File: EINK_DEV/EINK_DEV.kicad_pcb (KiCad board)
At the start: 2 copper layers, 50.5 x 46.5 mm, 76 parts, among them J1 FPC, J2 Conn_01x06, J3 Conn_01x02, J4 Conn_01x03, J5 Conn_ARM_SWD_TagConnect_TC2030, J6 UART, J7 Conn_Coaxial, J8 GPIO_Header_Dev, P1 USB_C_Plug_USB2.0, Q1 Si1304BDL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

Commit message: PCB gotowa
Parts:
- added J9: USER2, Connector_PinHeader_2.54mm:PinHeader_1x04_P2.54mm_Vertical, F.Cu at (127.5, 72.0)
- C1, C2, D2, L1: moved to B.Cu
- C10, C12, C31, C32, C5, C6, C7, C8, C9, R1, R2: moved to F.Cu
- FL1: value 2,4Ghz LP 50Ohm -> LP
- J2: value Conn_01x06 -> UART1; footprint Connector_PinHeader_2.54mm:PinHeader_1x06_P2.54mm_Vertical -> Connector_PinHeader_2.54mm:PinHeader_1x04_P2.54mm_Vertical
- J6: value UART -> LPUART
- J7: value Conn_Coaxial -> SMD
- J8: value GPIO_Header_Dev -> USER1
- JP1: footprint Connector_PinHeader_2.54mm:PinHeader_1x03_P2.54mm_Vertical -> Connector_PinHeader_2.54mm:PinHeader_1x03_P2.54mm_Horizontal
- Q1: value Si1304BDL -> NMOS
- TH1: value Thermistor_NTC -> THRMST
- moved C3 38.5 mm to (158.2, 114.5)
- moved D1 36.5 mm to (155.0, 110.8), turned to 90 degrees
- moved SW1 32.9 mm to (136.0, 104.0), turned to 180 degrees
- moved D3 31.6 mm to (162.6, 104.7)
- moved R13 29.9 mm to (123.7, 104.5), turned to 0 degrees
- moved C30 28.4 mm to (123.7, 107.0), turned to 180 degrees
- moved J6 28.2 mm to (119.5, 99.5), turned to 0 degrees
- moved R12 26.4 mm to (123.7, 102.0), turned to 0 degrees
- moved C4 26.0 mm to (162.5, 100.8), turned to -90 degrees
- moved J2 25.3 mm to (127.5, 87.0), turned to 0 degrees
- moved R15 25.1 mm to (128.7, 107.0), turned to 0 degrees
- moved R10 23.3 mm to (176.5, 75.7), turned to 90 degrees
- moved TH1 18.7 mm to (178.0, 103.2), turned to 90 degrees
- moved J8 13.5 mm to (119.5, 72.0)
- moved R1 12.1 mm to (175.5, 104.7), turned to 90 degrees
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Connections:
- J2 pad 1: Net-(J2-Pin_1) -> +3.3V
- J2 pad 4: Net-(J2-Pin_4) -> GND
- U1 pad 13: Net-(J2-Pin_2) -> Net-(J9-Pin_2)
- U1 pad 14: Net-(J2-Pin_3) -> Net-(J9-Pin_3)
- U1 pad 18: Net-(J2-Pin_4) -> Net-(J2-Pin_2)
- U1 pad 36: Net-(J2-Pin_5) -> Net-(J2-Pin_3)
- U1 pad 42: Net-(J2-Pin_6) -> Net-(J9-Pin_4)
- U1 pad 9: Net-(J2-Pin_1) -> Net-(J9-Pin_1)
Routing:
- net GND: track 274.2 -> 371.3 mm, vias 4 -> 9
- net Net-(J8-Pin_2): track 0.00 -> 73.5 mm, vias 0 -> 1
- net Net-(U1-PA3): track 0.00 -> 69.4 mm, vias 0 -> 1
- net Net-(J9-Pin_3): track 0.00 -> 60.7 mm, vias 0 -> 3
- net +3V3: track 115.2 -> 172.1 mm, vias 5 -> 12
- net Net-(J8-Pin_9): track 0.00 -> 51.3 mm, vias 0 -> 2
- net Net-(J5-SWO): track 0.00 -> 49.4 mm, vias 0 -> 1
- net Net-(J8-Pin_3): track 2.08 -> 51.0 mm, vias 0 -> 1
- net D+: track 0.00 -> 48.0 mm, vias 0 -> 2
- net Net-(D1-A): track 9.30 -> 56.9 mm, vias 0 -> 4
- net Net-(U1-PA2): track 0.00 -> 47.4 mm, vias 0 -> 1
- net Net-(J9-Pin_2): track 0.00 -> 47.1 mm, vias 0 -> 2
- net RESE: track 59.9 -> 12.8 mm, vias 2 -> 0
- net Net-(J9-Pin_1): track 0.00 -> 46.7 mm, vias 0 -> 2
- net D-: track 0.00 -> 46.5 mm, vias 0 -> 2
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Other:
- board size 50.5 x 46.5 mm -> 66.5 x 48.5 mm

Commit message: update
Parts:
- J3: footprint Connector_Molex:Molex_KK-254_AE-6410-02A_1x02_P2.54mm_Vertical -> Connector_PinHeader_2.54mm:PinHeader_1x02_P2.54mm_Vertical
- J4: footprint Connector:FanPinHeader_1x03_P2.54mm_Vertical -> Connector_PinHeader_2.54mm:PinHeader_1x03_P2.54mm_Horizontal
- U2 >: renamed from U2
- moved J4 0.23 mm to (178.5, 91.9), turned to 0 degrees
- turned J3 to -90 degrees
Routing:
- net Net-(J8-Pin_2): track 73.5 -> 56.4 mm
- net GND: track 371.3 -> 368.6 mm

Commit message: Uporzadkowanie komponentów HF
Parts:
- C1, C17, C18, C2, C26, C27, C30, C33, D2, L1, R12, R13, R15, Y1: moved to F.Cu
- FL1: value LP -> 2,4Ghz LP 50Ohm
- J3: footprint Connector_PinHeader_2.54mm:PinHeader_1x02_P2.54mm_Vertical -> Connector_Molex:Molex_KK-254_AE-6410-02A_1x02_P2.54mm_Vertical
- J4: footprint Connector_PinHeader_2.54mm:PinHeader_1x03_P2.54mm_Horizontal -> Connector:FanPinHeader_1x03_P2.54mm_Vertical
- J5: footprint Connector:Tag-Connect_TC2030-IDC-FP_2x03_P1.27mm_Vertical -> Connector_PinHeader_2.54mm:PinHeader_1x06_P2.54mm_Vertical
- J6: value LPUART -> LOW POWER UART
- J7: value SMD -> Conn_Coaxial
- Q1: value NMOS -> Si1304BDL
- TH1: value THRMST -> Thermistor_NTC
- U2: renamed from U2 >
- moved JP1 109.3 mm to (70.5, 99.8), turned to 180 degrees
- moved P1 106.5 mm to (73.4, 72.9), turned to 90 degrees
- moved R4 101.9 mm to (71.9, 87.2), turned to 180 degrees
- moved R10 99.9 mm to (76.8, 70.3), turned to -90 degrees
- moved D4 99.8 mm to (72.0, 91.0), turned to 0 degrees
- moved C12 99.5 mm to (74.8, 83.7), turned to -90 degrees
- moved C31 99.2 mm to (81.8, 68.8), turned to 90 degrees
- moved R9 98.1 mm to (77.0, 74.6), turned to 90 degrees
- moved R5 97.0 mm to (76.8, 83.8)
- moved C32 96.4 mm to (80.2, 68.8)
- moved J4 96.3 mm to (82.4, 98.5)
- moved J3 95.3 mm to (74.5, 99.0), turned to 0 degrees
- moved U2 94.1 mm to (79.2, 88.2), turned to 180 degrees
- moved TH1 93.8 mm to (84.8, 93.5), turned to 180 degrees
- moved U3 93.5 mm to (80.7, 73.6)
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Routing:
- net GND: track 368.6 -> 0.00 mm, vias 9 -> 0
- net +3V3: track 172.1 -> 0.00 mm, vias 12 -> 0
- net Net-(J2-Pin_2): track 75.6 -> 0.00 mm, vias 7 -> 0
- net Net-(D4-A): track 75.0 -> 0.00 mm, vias 7 -> 0
- net Net-(U1-PA3): track 69.4 -> 0.00 mm, vias 1 -> 0
- net Net-(D3-A): track 63.5 -> 0.00 mm, vias 1 -> 0
- net VBUS: track 61.0 -> 0.00 mm, vias 4 -> 0
- net Net-(J9-Pin_3): track 60.7 -> 0.00 mm, vias 3 -> 0
- net Net-(D1-A): track 56.9 -> 0.00 mm, vias 4 -> 0
- net Net-(J8-Pin_2): track 56.4 -> 0.00 mm, vias 1 -> 0
- net Net-(J8-Pin_7): track 53.6 -> 0.00 mm, vias 3 -> 0
- net Net-(J8-Pin_9): track 51.3 -> 0.00 mm, vias 2 -> 0
- net Net-(J8-Pin_3): track 51.0 -> 0.00 mm, vias 1 -> 0
- net Net-(J5-SWO): track 49.4 -> 0.00 mm, vias 1 -> 0
- net Net-(J8-Pin_1): track 49.3 -> 0.00 mm, vias 1 -> 0
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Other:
- board outline removed
- copper layers 2 -> 4

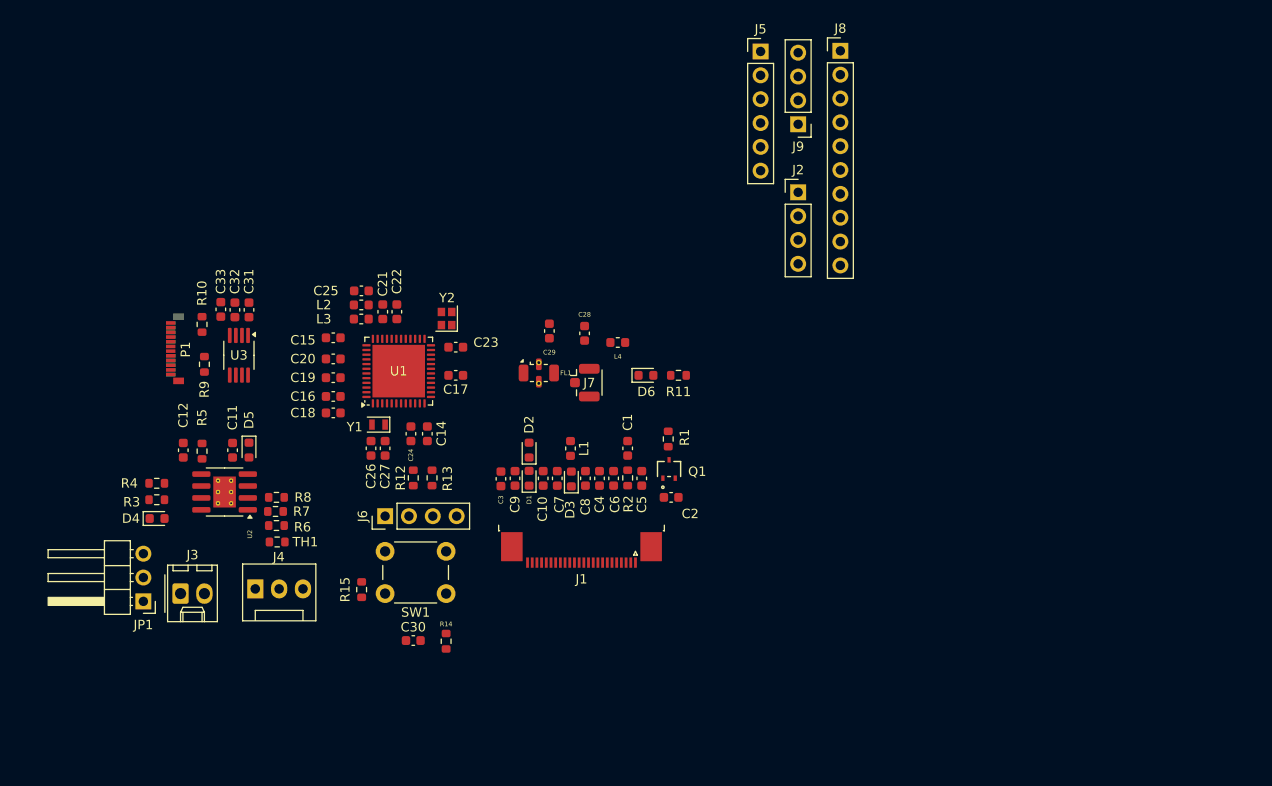
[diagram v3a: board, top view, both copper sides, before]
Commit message: Płytka prawie końcowa
 - prawidłowa impredancja
- prawidłowe warstwy GND i 3v3
- rozłożenie prawidłowe C 
- do poprawienia napisy
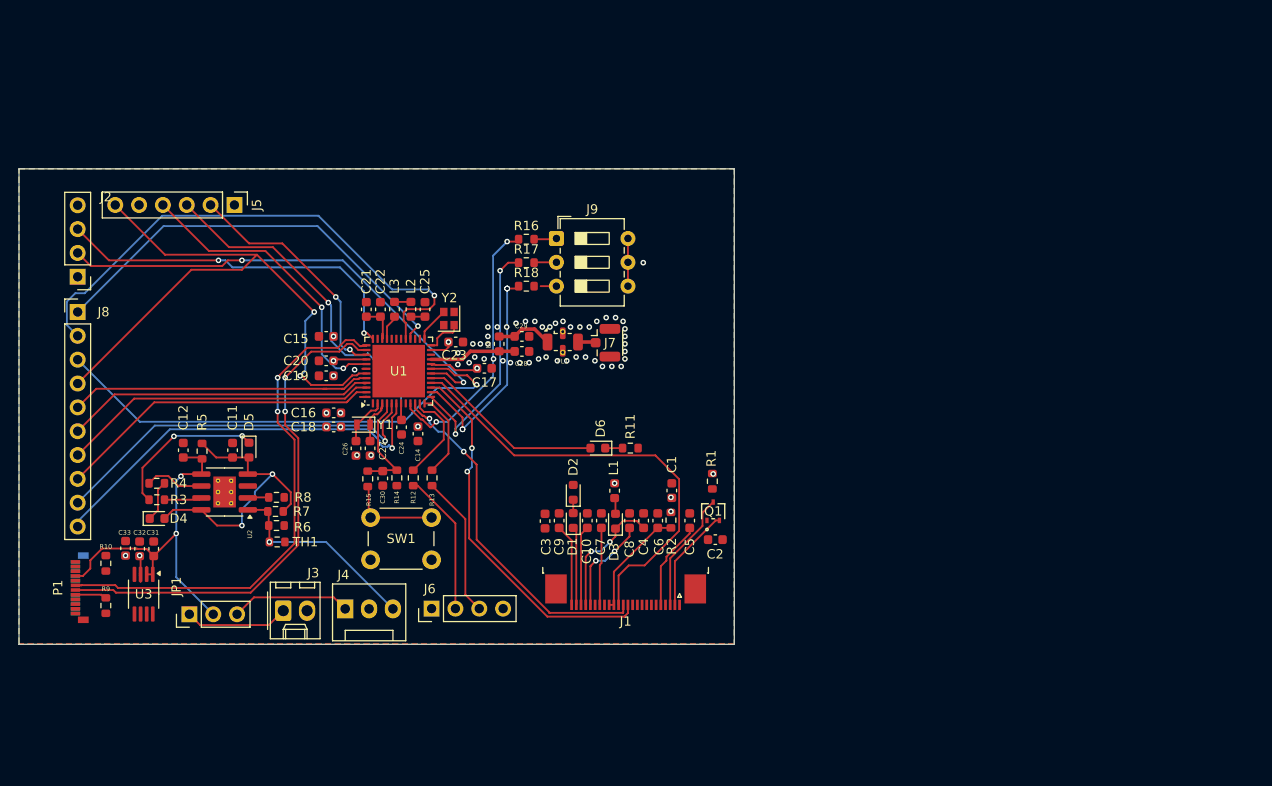
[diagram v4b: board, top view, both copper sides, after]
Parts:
- added R16: 220R, Resistor_SMD:R_0603_1608Metric, F.Cu at (111.3, 61.2)
- added R17: 220R, Resistor_SMD:R_0603_1608Metric, F.Cu at (111.3, 63.8)
- added R18: 220R, Resistor_SMD:R_0603_1608Metric, F.Cu at (111.3, 66.2)
- J9: footprint Connector_PinHeader_2.54mm:PinHeader_1x04_P2.54mm_Vertical -> Button_Switch_THT:SW_DIP_SPSTx03_Slide_6.7x9.18mm_W7.62mm_P2.54mm_LowProfile
- JP1: footprint Connector_PinHeader_2.54mm:PinHeader_1x03_P2.54mm_Horizontal -> Connector_PinHeader_2.54mm:PinHeader_1x03_P2.54mm_Vertical
- moved J8 85.9 mm to (63.5, 69.0)
- moved J2 77.3 mm to (63.5, 65.2), turned to 180 degrees
- moved J5 58.4 mm to (80.2, 57.6), turned to -90 degrees
- moved J9 28.5 mm to (114.5, 61.2), turned to 0 degrees
- moved R9 27.8 mm to (66.5, 100.3)
- moved R10 27.4 mm to (66.5, 95.8)
- moved C33 27.4 mm to (68.6, 94.2)
- moved P1 27.4 mm to (63.2, 98.4)
- moved U3 27.4 mm to (70.5, 99.1)
- moved C31 27.4 mm to (71.6, 94.2)
- moved C32 27.4 mm to (70.1, 94.2)
- moved R14 18.2 mm to (97.5, 86.7)
- moved C30 17.6 mm to (96.0, 86.7), turned to -90 degrees
- moved L4 12.6 mm to (108.4, 72.4), turned to 90 degrees
- moved R15 11.8 mm to (94.4, 86.8)
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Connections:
- J2 pad 1: +3.3V -> +3V3
- J6 pad 1: +3.3V -> +3V3
- J9 pad 1: Net-(J9-Pin_1) -> Net-(J9-Pad1)
- J9 pad 2: Net-(J9-Pin_2) -> Net-(J9-Pad2)
- J9 pad 3: Net-(J9-Pin_3) -> Net-(J9-Pad3)
- J9 pad 4: Net-(J9-Pin_4) -> +3V3
- SW1 pad 2: +3.3V -> +3V3
- U1 pad 13: Net-(J9-Pin_2) -> Net-(U1-PA4)
- U1 pad 14: Net-(J9-Pin_3) -> Net-(U1-PA5)
- U1 pad 42: Net-(J9-Pin_4) -> unconnected-(U1-PA15-Pad42)
- U1 pad 9: Net-(J9-Pin_1) -> Net-(U1-PA0)
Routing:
- net Net-(J5-SWO): track 0.00 -> 66.1 mm, vias 0 -> 2
- net Net-(J8-Pin_2): track 0.00 -> 58.0 mm, vias 0 -> 1
- net D-: track 0.00 -> 55.8 mm, vias 0 -> 2
- net D+: track 0.00 -> 55.2 mm, vias 0 -> 2
- net Net-(J8-Pin_3): track 0.00 -> 52.6 mm, vias 0 -> 1
- net Net-(J2-Pin_2): track 0.00 -> 51.3 mm, vias 0 -> 2
- net SDA_SCREEN: track 0.00 -> 47.7 mm
- net Net-(J8-Pin_1): track 0.00 -> 46.1 mm, vias 0 -> 1
- net Net-(J8-Pin_10): track 0.00 -> 44.2 mm, vias 0 -> 1
- net Net-(J8-Pin_9): track 0.00 -> 41.3 mm, vias 0 -> 1
- net CS#_SCREEN: track 0.00 -> 40.1 mm, vias 0 -> 2
- net VBUS: track 0.00 -> 39.8 mm, vias 0 -> 2
- net Net-(J2-Pin_3): track 0.00 -> 38.9 mm, vias 0 -> 2
- net SWD_NRST: track 0.00 -> 37.8 mm, vias 0 -> 1
- net SCL_SCREEN: track 0.00 -> 37.6 mm, vias 0 -> 2
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- added copper zone on In2.Cu, net +3V3
- added copper zone on B.Cu, net GND
- added copper zone on F.Cu, net GND
- added copper zone on In1.Cu, net GND
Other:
- board outline added: 76.2 x 50.7 mm
